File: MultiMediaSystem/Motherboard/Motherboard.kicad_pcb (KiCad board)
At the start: 4 copper layers, 173.4 x 157.7 mm, 43 parts, among them J1 Wire Harness, J10 RF_EN, J14 5V_1, J15 RPI_Buck, J16 AUSB2-4599, J17 Illum/Dim, J18 5V_2, J19 GP_Buck, J2 Vmem Jumper, J20 5V_3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

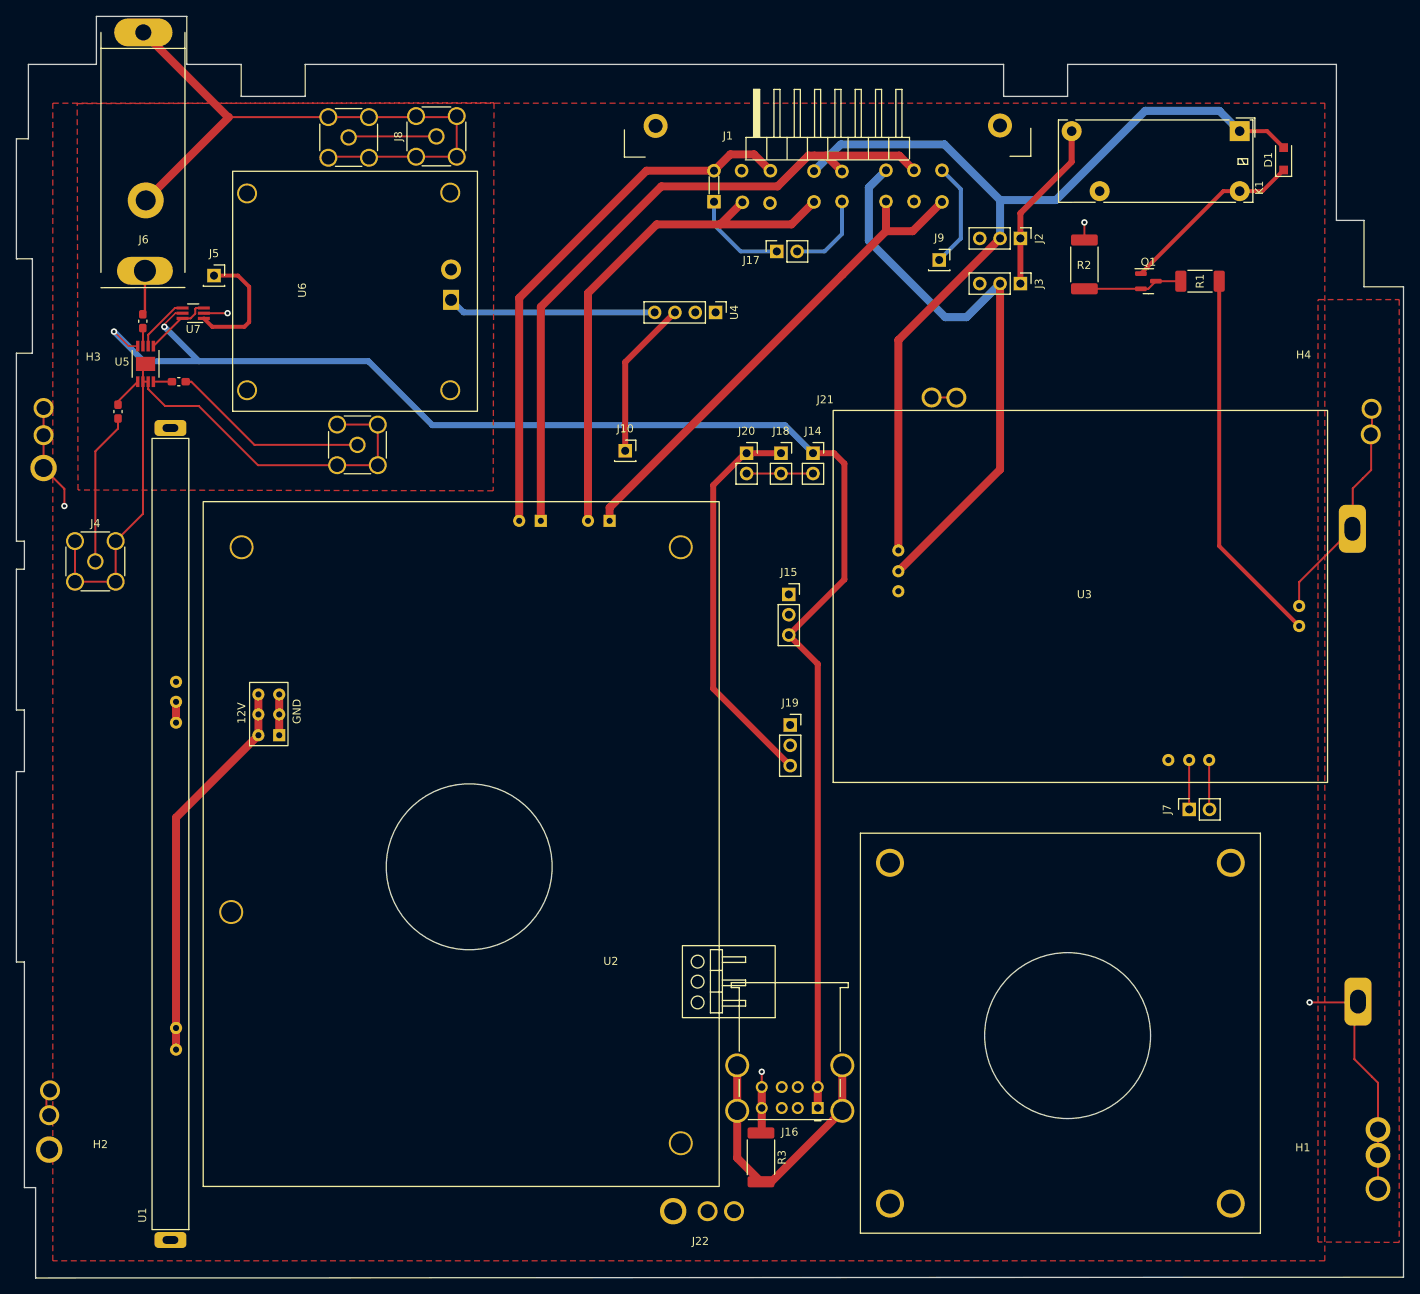
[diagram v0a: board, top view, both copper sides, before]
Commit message: Adjusted Motherboard Pinouts
Motherboard pinout's were slightly off. This corrects that problem.
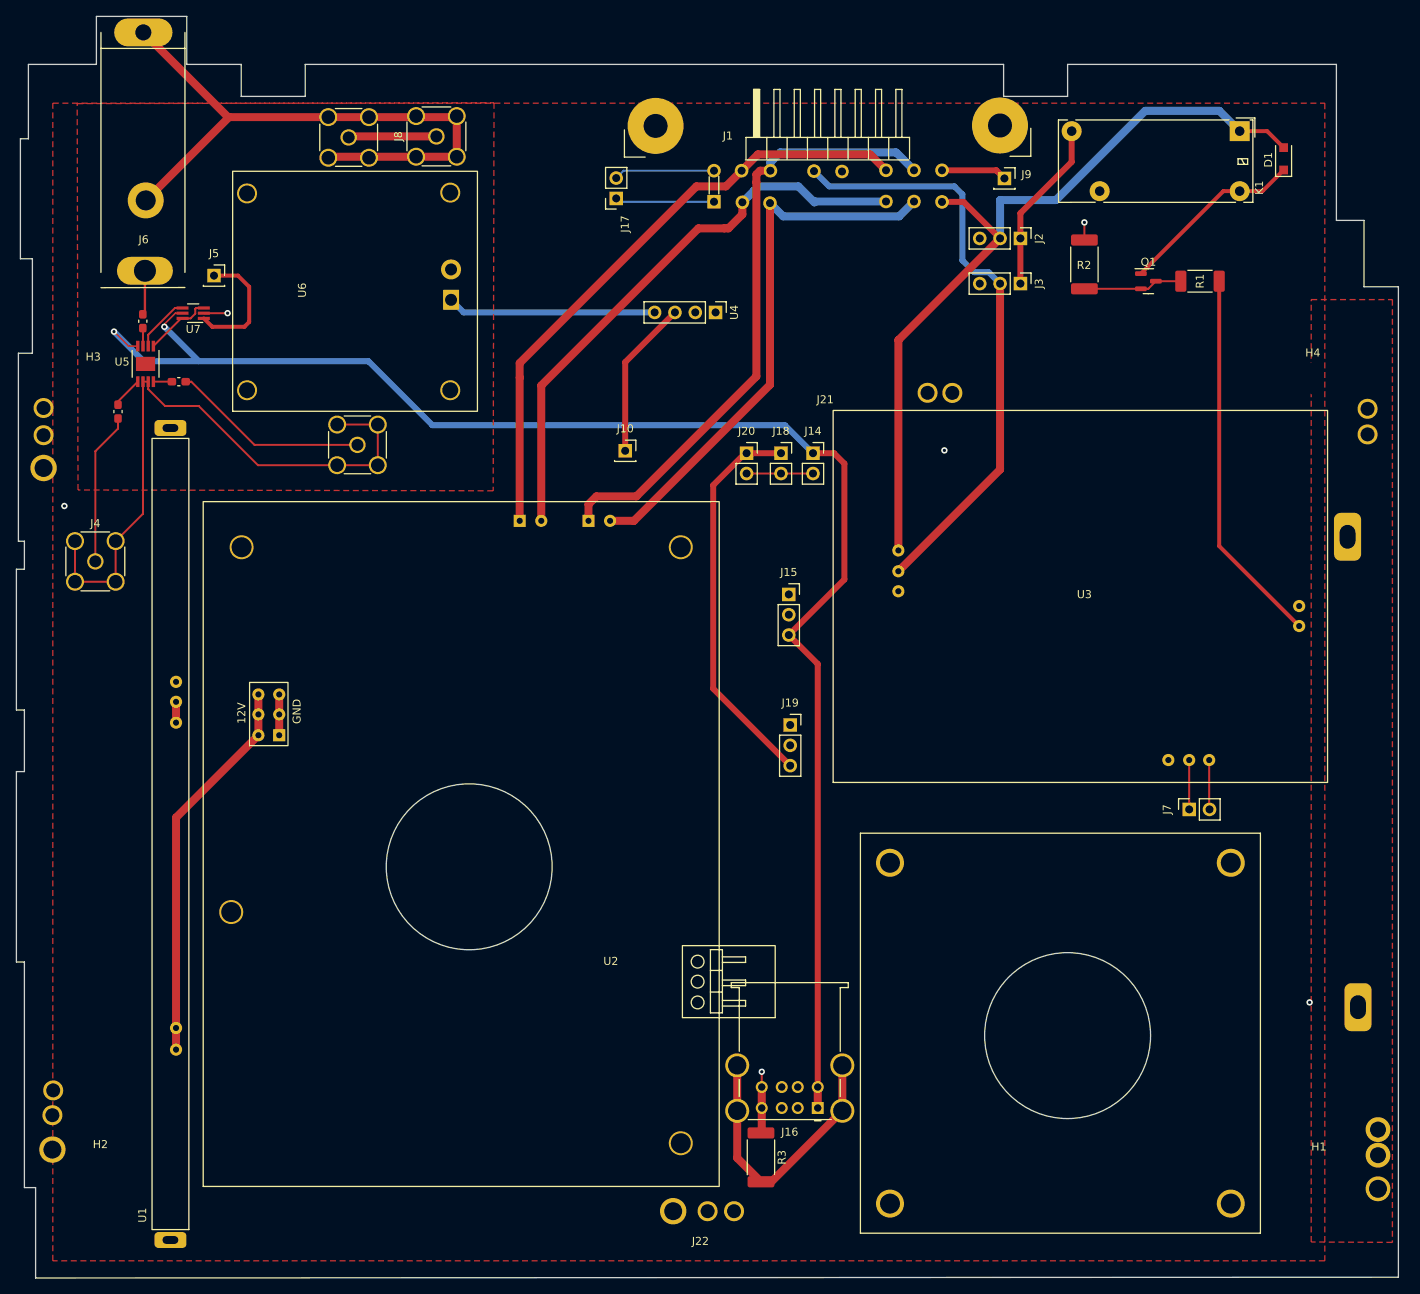
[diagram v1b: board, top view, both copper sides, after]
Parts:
- moved J17 21.1 mm to (199.5, 73.8), turned to 180 degrees
- moved J9 13.1 mm to (248.0, 71.2)
- moved H1 2.00 mm to (287.2, 195.5)
- moved H4 1.18 mm to (286.5, 96.2)
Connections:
- J1 pad 10: FrontSpkr_R- -> Vacc
- J1 pad 11: FrontSpkr_L- -> GND
- J1 pad 12: Vacc -> FrontSpkr_R-
- J1 pad 13: GND -> FrontSpkr_L-
- J1 pad 14: FrontSpkr_R- -> Antenna_Pwr
- J1 pad 4: unconnected-(J1-Pad4) -> FrontSpkr_R+
- J1 pad 5: unconnected-(J1-Pad5) -> FrontSpkr_L+
- J1 pad 6: FrontSpkr_R+ -> Vmem
- J1 pad 7: FrontSpkr_L+ -> Dim
- J1 pad 8: Vmem -> FrontSpkr_R-
- J1 pad 9: Dim -> FrontSpkr_L-
- J21 pad 1: GND -> unconnected-(J21-Pad1)
- J22 pad 1: GND -> unconnected-(J22-Pad1)
- U5 pad EPAD: RF_gnd -> unconnected-(U5-PadEPAD)
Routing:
- net GND: track 104.9 -> 26.4 mm, vias 5 -> 6
- net Vmem: track 118.6 -> 100.2 mm
- net FrontSpkr_L-: track 62.7 -> 77.3 mm
- net FrontSpkr_R-: track 86.6 -> 77.1 mm
- net Antenna_Pwr: track 13.3 -> 8.22 mm
- net FrontSpkr_R+: track 67.5 -> 72.1 mm
- net FrontSpkr_L+: track 65.3 -> 69.2 mm
- net RF_gnd: track 162.7 -> 160.4 mm
- net Vacc: track 73.0 -> 75.1 mm
- net Dim: track 10.6 -> 12.6 mm
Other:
- board size 173.4 x 157.7 mm -> 172.8 x 157.7 mm
- board text added: "MountingHole Error: Too far away from right wall"

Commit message: Updated all designs
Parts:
- removed J7: PwrCtrl_in, Connector_PinSocket_2.54mm:PinSocket_1x02_P2.54mm_Vertical
- J15, J19: footprint Connector_PinSocket_2.54mm:PinSocket_1x03_P2.54mm_Vertical -> Custom:5V_Reg_Footprint_VertMnt
- moved J15 54.1 mm to (274.6, 131.1), turned to 90 degrees
- moved U3 50.4 mm to (236.3, 97.3), turned to -90 degrees
- moved J14 45.1 mm to (267.5, 93.3), turned to -90 degrees
- moved D1 25.0 mm to (259.5, 60.0), turned to 180 degrees
- moved J19 24.9 mm to (218.0, 114.8), turned to 180 degrees
- moved K1 21.7 mm to (255.7, 63.6), turned to 0 degrees
- moved U2 21.4 mm to (210.3, 176.0)
- moved Q1 19.6 mm to (268.1, 64.6)
- moved R2 15.4 mm to (272.2, 76.1), turned to 0 degrees
- moved J10 14.1 mm to (206.8, 92.6)
- moved H7 13.4 mm to (286.8, 148.5)
- moved U1 11.2 mm to (142.6, 192.2)
- moved H5 10.4 mm to (227.5, 148.4)
- moved R3 8.77 mm to (221.7, 201.3), turned to 90 degrees
- moved H6 7.08 mm to (282.8, 196.6)
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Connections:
- J16 pad 1: 5V -> 5V_GP
- J16 pad 5: 5V -> 5V_GP
- U5 pad 4: 5V -> 5V_GP
- U7 pad 5: 5V -> 5V_GP
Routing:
- net Vsrc: track 2.60 -> 296.7 mm
- net 5V: track 196.0 -> 37.2 mm, vias 2 -> 0
- net 5V_GP: track 49.2 -> 201.2 mm, vias 0 -> 2
- net AudioPwr: track 48.7 -> 12.0 mm
- net FrontSpkr_R+: track 72.1 -> 101.6 mm
- net FrontSpkr_R-: track 77.1 -> 106.5 mm
- net Radio_EN: track 19.9 -> 4.61 mm
- net Net-(D1-Pad1): track 23.2 -> 8.51 mm
- net Vacc: track 75.1 -> 63.7 mm
- net Vdd: track 21.7 -> 11.5 mm
- net Vmem: track 100.2 -> 92.2 mm
- net Net-(Q1-Pad2): track 12.4 -> 20.0 mm
- net Net-(J16-Pad9): track 35.3 -> 28.5 mm
- net UART_TX: track 6.19 -> 0.00 mm
- net UART_RX: track 6.17 -> 0.00 mm
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- added copper zone on B.Cu, net 5V
- added copper zone on B.Cu, net AudioPwr
- added copper zone on F.Cu, net AudioPwr
- added copper zone on B.Cu, net GND
- added copper zone on F.Cu, net Vdd
- added copper zone on B.Cu, net Vsrc
- removed copper zone on In1.Cu, net GND
- removed copper zone on In2.Cu, net Vsrc
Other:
- board size 172.8 x 157.7 mm -> 172.1 x 157.6 mm
- copper layers 4 -> 2
- board text removed: "MountingHole Error: Too far away from right wall"
